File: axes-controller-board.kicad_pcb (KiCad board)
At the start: 2 copper layers, 185.1 x 102.9 mm, 139 parts, among them IC1 TPS5450QDDARQ1, IC2 ACS37800KMACTR-030B3-SPI, IC3 ACS37800KMACTR-030B3-SPI, IC4 ACS37800KMACTR-030B3-SPI, IC5 STM32H723ZGT6, J1 Conn_ST_STDC14, J10 Conn_01x08, J11 Conn_01x04, J12 Conn_01x08, J13 Conn_01x04, J14 Conn_01x08, J15 Conn_01x08, J16 Conn_01x04, J17 Conn_01x08, J18 Conn_01x08, J19 Conn_01x04, J2 Conn_01x03, J20 Conn_01x08, J21 Conn_01x08, J22 Conn_01x04, J23 Conn_01x08, J24 Conn_01x08, J25 Conn_01x04, J26 Conn_01x08, J27 Raspberry_Pi_2_3, J28 DC1, J29 DC2, J3 Conn_01x03, J30 DC3, J31 Conn_01x08, J32 Conn_01x08, J33 DC1, J34 Conn_01x08, J35 Conn_01x08, J36 Conn_01x08, J4 Conn_01x03, J5 DRIVER, J6 NTC, J7 DRIVER, J8 NTC, J9 Conn_01x08, SW1 RESET, U1 LM1117MP-3.3, U3 UA9637A, U5 UA9637A, U7 UA9637A, Y1 16MHz

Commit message: feat: endstops integration
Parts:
- added J37: ENDSTOP, Connector_PinHeader_2.54mm:PinHeader_1x02_P2.54mm_Vertical, F.Cu at (195.8, 102.2)
- added J38: ENDSTOP, Connector_PinHeader_2.54mm:PinHeader_1x02_P2.54mm_Vertical, F.Cu at (195.7, 87.9)
- added J39: ENDSTOP, Connector_PinHeader_2.54mm:PinHeader_1x02_P2.54mm_Vertical, F.Cu at (195.5, 73.3)
- moved J6 15.8 mm to (163.8, 66.2)
- moved J8 15.8 mm to (168.5, 66.2)
- moved J5 15.8 mm to (173.2, 66.2)
- moved J7 15.8 mm to (177.8, 66.2)
- moved F1 1.51 mm to (86.0, 73.1)
- moved C1 1.16 mm to (88.3, 73.9), turned to -90 degrees
- turned J3 to 90 degrees
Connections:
- IC5 pad 90: unconnected-(IC5-PG5-Pad90) -> /MCU/ES_Y2
- IC5 pad 91: unconnected-(IC5-PG6-Pad91) -> /MCU/ES_Y1
- IC5 pad 92: unconnected-(IC5-PG7-Pad92) -> /MCU/ES_X
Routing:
- net +5V: track 21.0 -> 190.4 mm
- net +3V3: track 48.9 -> 59.0 mm
- net Net-(U1-VI): track 0.00 -> 4.06 mm

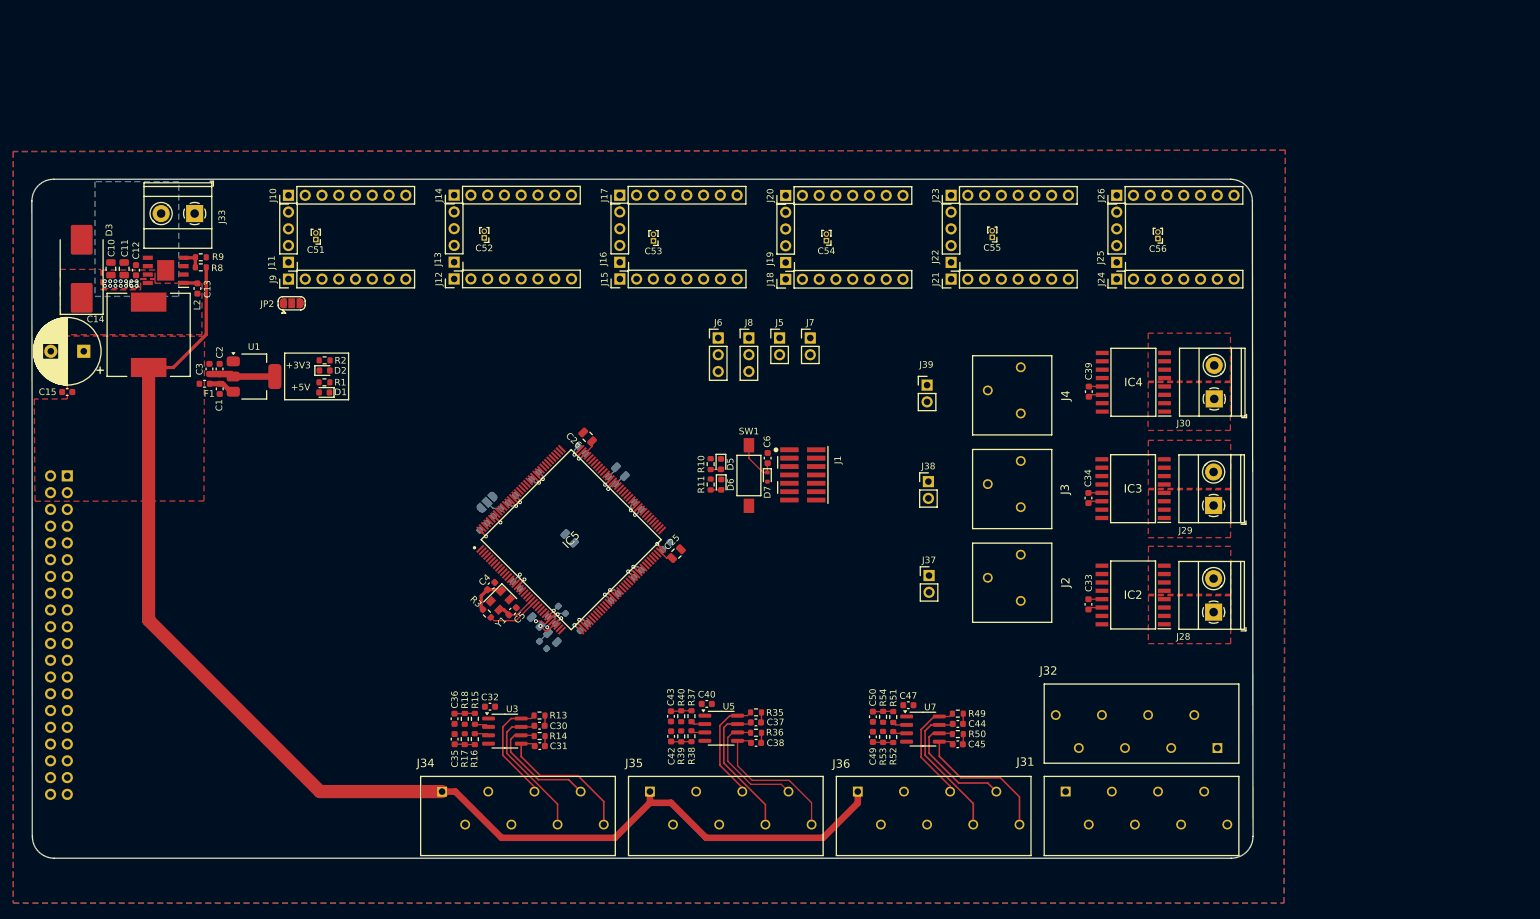
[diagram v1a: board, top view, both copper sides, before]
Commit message: feat: spi and 3v3 routing
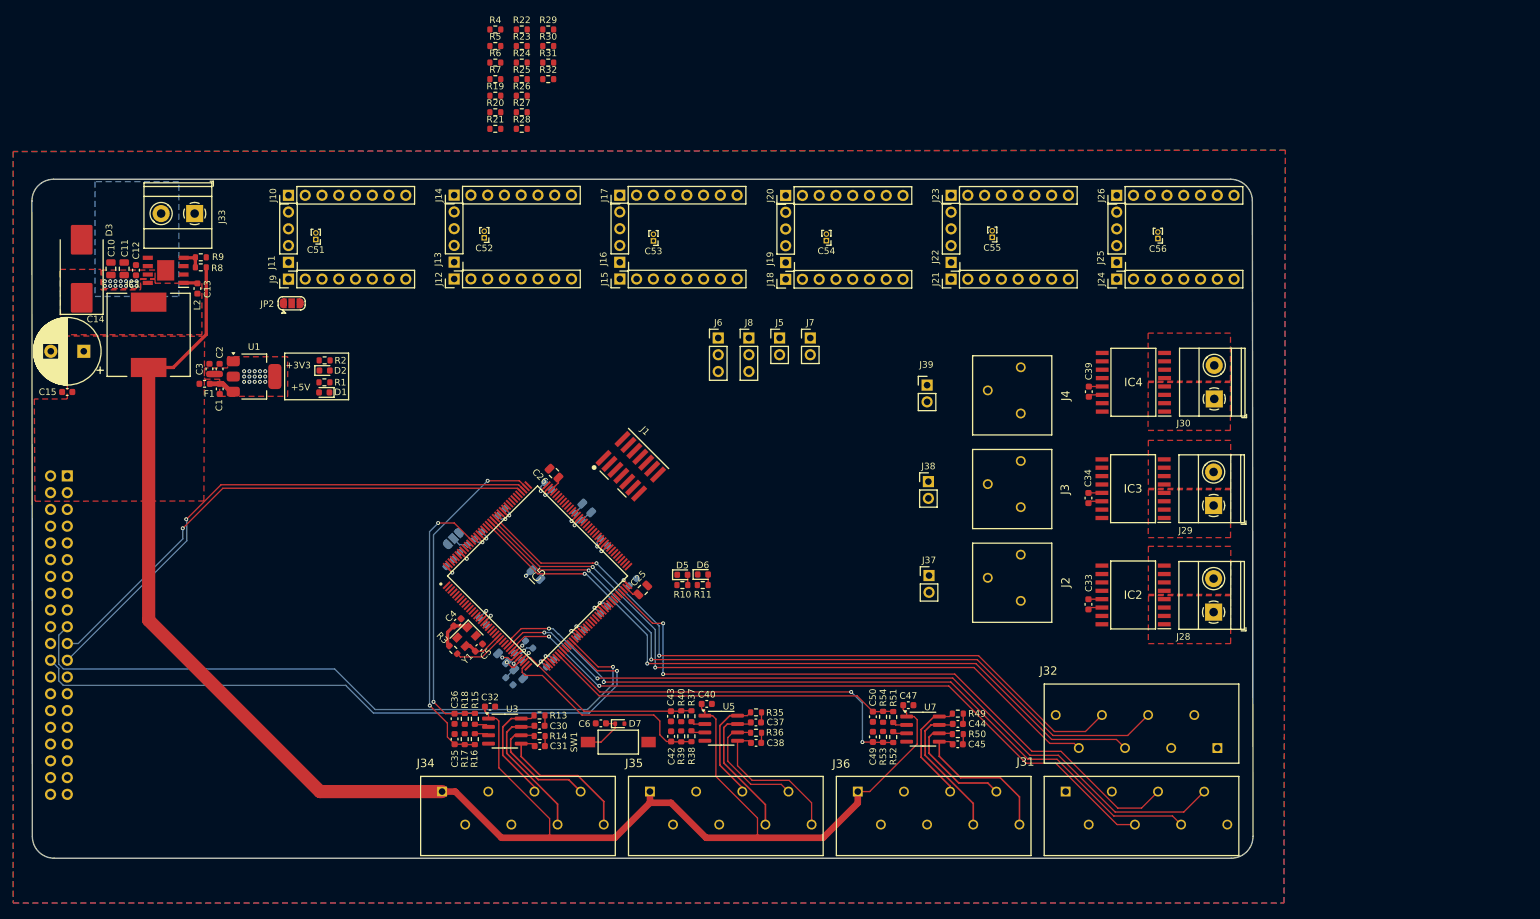
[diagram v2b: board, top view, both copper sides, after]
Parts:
- added R19: R, Resistor_SMD:R_0603_1608Metric, F.Cu at (130.1, 29.4)
- added R20: R, Resistor_SMD:R_0603_1608Metric, F.Cu at (130.1, 31.9)
- added R21: R, Resistor_SMD:R_0603_1608Metric, F.Cu at (130.1, 34.5)
- added R22: R, Resistor_SMD:R_0603_1608Metric, F.Cu at (134.1, 19.4)
- added R23: R, Resistor_SMD:R_0603_1608Metric, F.Cu at (134.1, 21.9)
- added R24: R, Resistor_SMD:R_0603_1608Metric, F.Cu at (134.1, 24.4)
- added R25: R, Resistor_SMD:R_0603_1608Metric, F.Cu at (134.1, 26.9)
- added R26: R, Resistor_SMD:R_0603_1608Metric, F.Cu at (134.1, 29.4)
- added R27: R, Resistor_SMD:R_0603_1608Metric, F.Cu at (134.1, 31.9)
- added R28: R, Resistor_SMD:R_0603_1608Metric, F.Cu at (134.1, 34.5)
- added R29: R, Resistor_SMD:R_0603_1608Metric, F.Cu at (138.1, 19.4)
- added R30: R, Resistor_SMD:R_0603_1608Metric, F.Cu at (138.1, 21.9)
- added R31: R, Resistor_SMD:R_0603_1608Metric, F.Cu at (138.1, 24.4)
- added R32: R, Resistor_SMD:R_0603_1608Metric, F.Cu at (138.1, 26.9)
- added R4: R, Resistor_SMD:R_0603_1608Metric, F.Cu at (130.1, 19.4)
- added R5: R, Resistor_SMD:R_0603_1608Metric, F.Cu at (130.1, 21.9)
- added R6: R, Resistor_SMD:R_0603_1608Metric, F.Cu at (130.1, 24.4)
- added R7: R, Resistor_SMD:R_0603_1608Metric, F.Cu at (130.1, 26.9)
- moved C6 47.5 mm to (146.1, 124.6), turned to 180 degrees
- moved SW1 45.0 mm to (148.7, 127.4), turned to 180 degrees
- moved D7 43.6 mm to (148.9, 124.6), turned to 0 degrees
- moved J1 26.1 mm to (150.6, 85.6), turned to -45 degrees
- moved R10 18.8 mm to (158.4, 103.6), turned to 180 degrees
- moved D5 17.8 mm to (158.4, 102.0), turned to 0 degrees
- moved R11 15.3 mm to (161.5, 103.6), turned to 180 degrees
- moved D6 13.9 mm to (161.5, 102.0), turned to 0 degrees
- moved C20 7.50 mm to (146.6, 97.1)
- moved C8 7.50 mm to (146.5, 107.4)
- moved C18 7.50 mm to (127.5, 96.1)
- moved R12 7.50 mm to (125.3, 98.1)
- moved C16 7.50 mm to (133.6, 114.5)
- moved C17 7.50 mm to (150.9, 103.2)
- moved C19 7.50 mm to (138.4, 115.5)
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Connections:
- IC5 pad 114: /STEP_P1 -> Net-(IC5-PD0)
- IC5 pad 115: /DIR_P2 -> Net-(IC5-PD1)
- IC5 pad 117: /STEP_P2 -> Net-(IC5-PD3)
- IC5 pad 118: /DIR_P2 -> Net-(IC5-PD4)
- IC5 pad 141: /STEP_Z1 -> Net-(IC5-PE0)
- IC5 pad 142: /DIR_Z1 -> Net-(IC5-PE1)
- IC5 pad 2: /STEP_Z2 -> Net-(IC5-PE3)
- IC5 pad 3: /DIR_Z2 -> Net-(IC5-PE4)
- IC5 pad 58: /DIR_F -> Net-(IC5-PE7)
- IC5 pad 59: /STEP_F -> Net-(IC5-PE8)
- IC5 pad 60: /MCU/X_DC_PWM_1 -> Net-(IC5-PE9)
- IC5 pad 64: /MCU/X_DC_PWM_2 -> Net-(IC5-PE11)
- IC5 pad 66: /MCU/Y1_DC_PWM_1 -> Net-(IC5-PE13)
- IC5 pad 67: /MCU/Y1_DC_PWM_2 -> Net-(IC5-PE14)
- IC5 pad 79: /DIR_YAW -> Net-(IC5-PD10)
- IC5 pad 80: /STEP_YAW -> Net-(IC5-PD11)
- IC5 pad 96: /MCU/Y2_DC_PWM_1 -> Net-(IC5-PC6)
- IC5 pad 97: /MCU/Y2_DC_PWM_2 -> Net-(IC5-PC7)
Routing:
- net /MCU/SPI2_MISO: track 0.00 -> 119.1 mm, vias 0 -> 2
- net /MCU/SPI1_CSS: track 0.00 -> 116.6 mm, vias 0 -> 2
- net /MCU/SPI2_MOSI: track 0.00 -> 116.1 mm, vias 0 -> 2
- net /MCU/SPI1_SCK: track 0.00 -> 113.0 mm, vias 0 -> 2
- net /MCU/SPI1_MOSI: track 0.00 -> 109.0 mm, vias 0 -> 2
- net /MCU/SPI2_CSS: track 0.00 -> 107.2 mm, vias 0 -> 2
- net /MCU/SPI1_MISO: track 0.00 -> 106.4 mm, vias 0 -> 2
- net /MCU/SPI3_MOSI: track 0.00 -> 105.0 mm, vias 0 -> 1
- net /MCU/SPI3_CSS: track 0.00 -> 103.0 mm, vias 0 -> 1
- net /MCU/SPI2_SCK: track 0.00 -> 100.4 mm, vias 0 -> 2
- net /MCU/SPI3_SCK: track 0.00 -> 82.5 mm, vias 0 -> 1
- net /MCU/SPI3_MISO: track 0.00 -> 79.7 mm, vias 0 -> 1
- net +5V: track 190.4 -> 258.9 mm
- net /MCU/MY2_B: track 3.11 -> 59.5 mm, vias 0 -> 2
- net /MCU/MY2_A: track 3.11 -> 54.3 mm
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- added copper zone on F.Cu, net +3V3
- added copper zone on In1.Cu, net +3V3
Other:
- copper layers 2 -> 4

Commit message: fix: 33R resistors
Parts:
- moved R29 90.8 mm to (150.4, 109.4), turned to 135 degrees
- moved R6 90.8 mm to (146.0, 113.8), turned to -45 degrees
- moved R7 87.4 mm to (147.1, 112.7), turned to 135 degrees
- moved R30 87.4 mm to (151.5, 108.3), turned to 135 degrees
- moved R31 86.8 mm to (149.3, 110.5), turned to 135 degrees
- moved R32 85.3 mm to (148.2, 111.6), turned to -45 degrees
- moved R22 79.5 mm to (119.6, 97.6), turned to -45 degrees
- moved R4 78.7 mm to (150.7, 95.4), turned to 45 degrees
- moved R19 78.1 mm to (120.1, 106.9), turned to -135 degrees
- moved R5 77.7 mm to (151.8, 96.5), turned to 45 degrees
- moved R20 76.6 mm to (121.2, 108.0), turned to 45 degrees
- moved R23 67.7 mm to (128.4, 89.4), turned to 135 degrees
- moved R24 66.4 mm to (127.3, 90.5), turned to -45 degrees
- moved R21 62.7 mm to (120.7, 96.5), turned to 135 degrees
- moved R25 61.5 mm to (129.5, 88.3), turned to -45 degrees
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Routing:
- net Net-(U1-VI): track 4.06 -> 22.0 mm
- net +3V3: track 52.9 -> 60.7 mm
- net /MCU/MX_A: track 50.1 -> 54.1 mm
- net /MCU/SPI3_MISO: track 79.7 -> 82.4 mm
- net /MCU/SPI3_SCK: track 82.5 -> 85.2 mm
- net Net-(D2-A): track 0.00 -> 1.55 mm
- net Net-(D1-A): track 0.00 -> 1.53 mm
- added copper zone on In2.Cu, net +3V3
- added copper zone on In1.Cu, net GND
- removed copper zone on In1.Cu, net +3V3

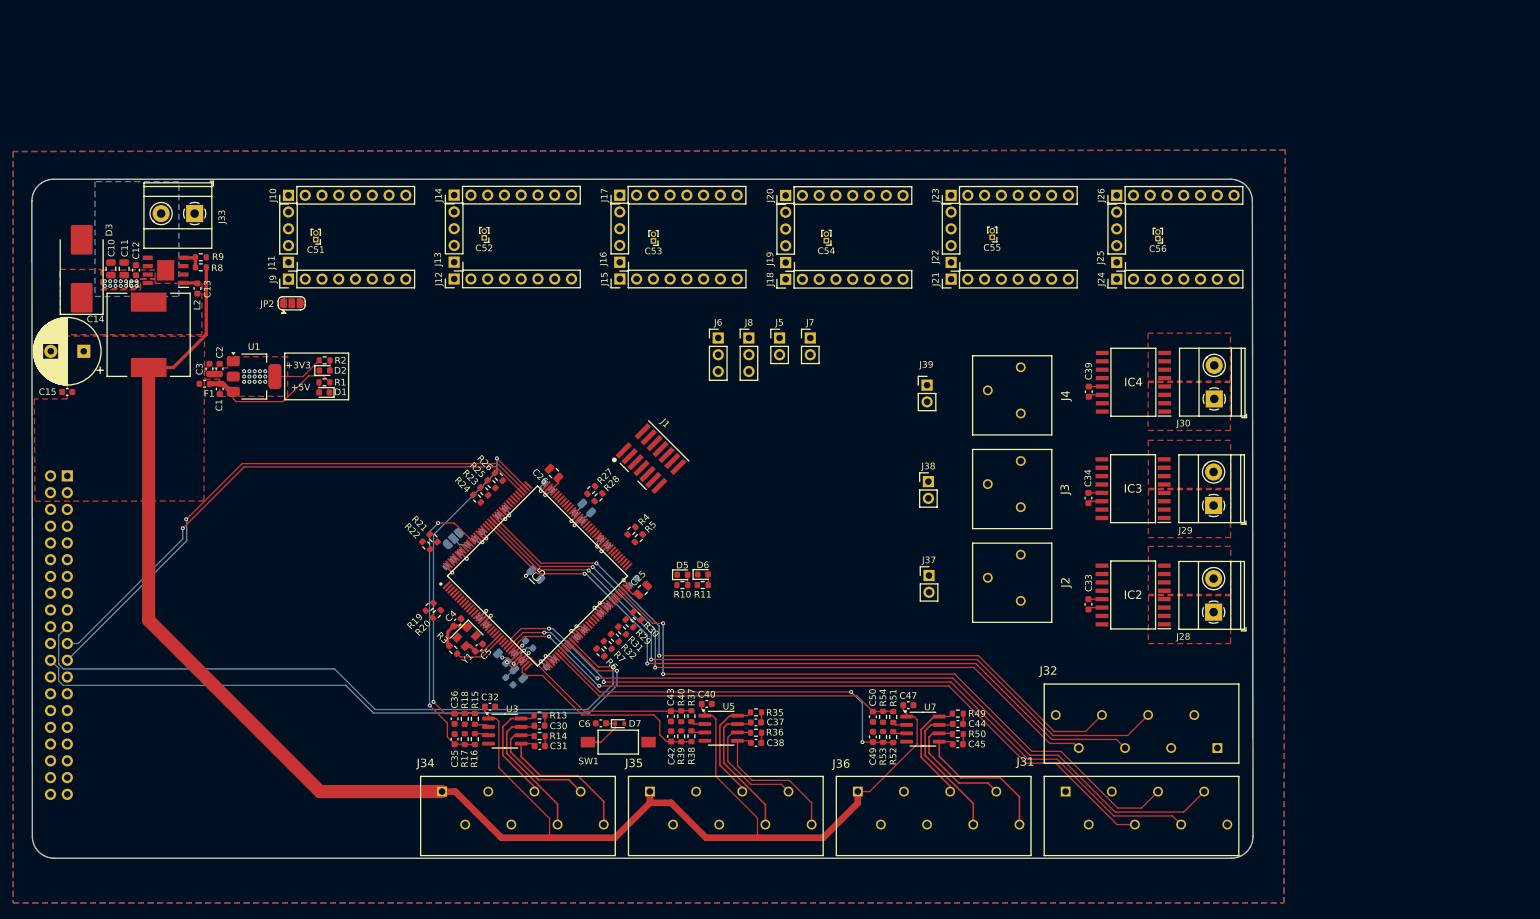
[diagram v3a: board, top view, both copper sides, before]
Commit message: feat: spi4 connections
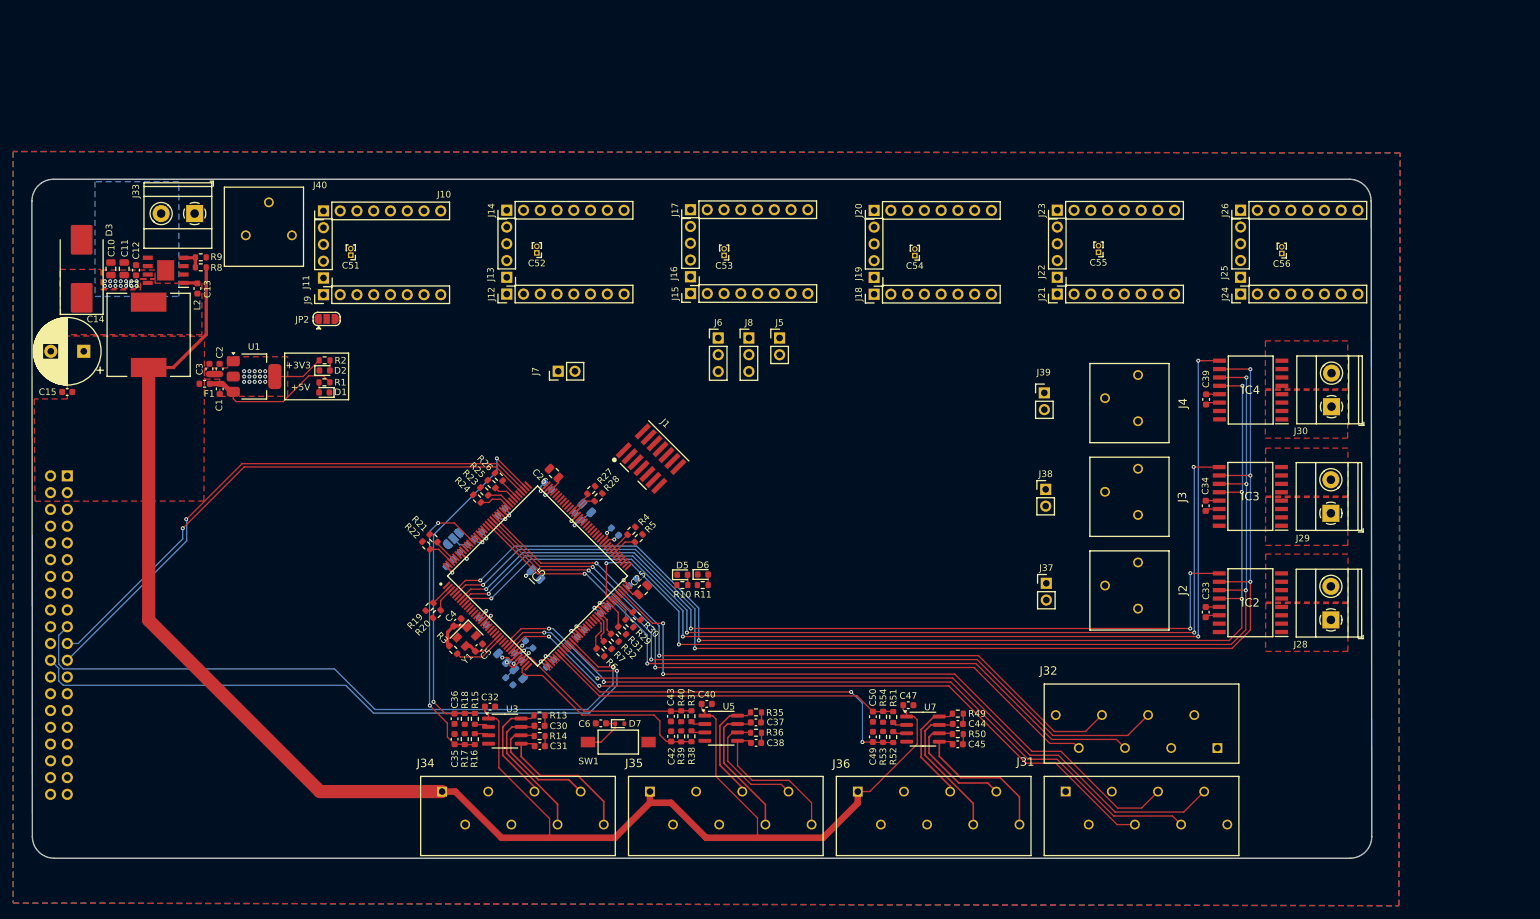
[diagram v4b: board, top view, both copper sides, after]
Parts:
- added J40: Conn_01x03, Local:1985205, F.Cu at (95.0, 49.3)
- moved J7 38.5 mm to (139.6, 71.2), turned to 90 degrees
- moved C56 18.9 mm to (249.3, 53.4)
- moved J24 18.9 mm to (243.0, 59.5)
- moved J25 18.9 mm to (243.0, 57.0)
- moved J26 18.9 mm to (243.0, 46.8)
- moved J30 17.8 mm to (256.8, 76.6)
- moved C33 17.8 mm to (237.7, 107.7)
- moved C34 17.8 mm to (237.7, 91.6)
- moved C39 17.8 mm to (237.8, 75.5)
- moved IC2 17.8 mm to (244.5, 106.3)
- moved IC3 17.8 mm to (244.5, 90.2)
- moved IC4 17.8 mm to (244.5, 74.0)
- moved J2 17.8 mm to (226.2, 104.4)
- moved J28 17.8 mm to (256.7, 108.9)
- moved J29 17.8 mm to (256.7, 92.7)
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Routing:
- net /Sensors/SPI4_MOSI: track 0.00 -> 188.5 mm, vias 0 -> 5
- net /Sensors/SPI4_MISO: track 0.00 -> 179.0 mm, vias 0 -> 5
- net /MCU/SPI4_CSS_Y2: track 0.00 -> 166.0 mm, vias 0 -> 4
- net /Sensors/SPI4_SCK: track 0.00 -> 162.6 mm, vias 0 -> 5
- net /MCU/SPI4_CSS_Y1: track 0.00 -> 149.6 mm, vias 0 -> 4
- net /MCU/SPI4_CSS_X: track 0.00 -> 132.7 mm, vias 0 -> 4
- net Net-(IC5-PE7): track 0.00 -> 5.35 mm
- net Net-(IC5-PD4): track 0.00 -> 4.62 mm
- net Net-(IC5-PE8): track 0.00 -> 4.58 mm
- net Net-(IC5-PE1): track 0.00 -> 4.01 mm
- net Net-(IC5-PE11): track 0.00 -> 3.97 mm
- net Net-(IC5-PE9): track 0.00 -> 3.79 mm
- net Net-(IC5-PD3): track 0.00 -> 3.78 mm
- net Net-(IC5-PE13): track 0.00 -> 3.77 mm
- net Net-(IC5-PD10): track 0.00 -> 3.76 mm
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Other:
- board size 185.1 x 102.9 mm -> 203.1 x 102.9 mm
